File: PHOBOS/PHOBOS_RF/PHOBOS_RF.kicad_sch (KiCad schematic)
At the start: 0 parts

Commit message: RF Board schematic began
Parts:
- added AE1, AE2, AE3, AE4: Antenna, symbol Device:Antenna
- added J1: RF_IN, SMA_J_P_GF_RA_SM1:SAMTEC_SMA-J-P-GF-RA-SM1, symbol Connector:Conn_Coaxial
- added J7: Conn_01x05, Connector_JST:JST_PH_B5B-PH-K_1x05_P2.00mm_Vertical, symbol Connector_Generic:Conn_01x05
- added U1, U2, U3, U4: (no value), symbol JSPHS-2484+:JSPHS-2484+
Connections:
- new net: AE3.1 (A), U3.7 (RF_OUT)
- new net: AE1.1 (A), U1.7 (RF_OUT)
- new net: J1.1 (In), U1.1 (RF_IN), U2.1 (RF_IN), U3.1 (RF_IN), U4.1 (RF_IN)
- new net: AE2.1 (A), U2.7 (RF_OUT)
- new net: AE4.1 (A), U4.7 (RF_OUT)
- new net GND: J1.2 (Ext), J1.3, J1.4, J1.5, J7.5 (Pin_5), U1.10 (GND), U1.11 (GND), U1.12 (GND), U1.13 (GND), U1.14 (GND), U1.2 (GND), U1.3 (GND), U1.5 (GND), U1.8 (GND), U1.9 (GND), U2.10 (GND), U2.11 (GND), U2.12 (GND), U2.13 (GND), U2.14 (GND), U2.2 (GND), U2.3 (GND), U2.5 (GND), U2.8 (GND), U2.9 (GND), U3.10 (GND), U3.11 (GND), U3.12 (GND), U3.13 (GND), U3.14 (GND), U3.2 (GND), U3.3 (GND), U3.5 (GND), U3.8 (GND), U3.9 (GND), U4.10 (GND), U4.11 (GND), U4.12 (GND), U4.13 (GND), U4.14 (GND), U4.2 (GND), U4.3 (GND), U4.5 (GND), U4.8 (GND), U4.9 (GND)
- new net PS1: J7.1 (Pin_1), U1.4 (BIAS), U1.6 (BIAS)
- new net PS2: J7.2 (Pin_2), U2.4 (BIAS), U2.6 (BIAS)
- new net PS3: J7.3 (Pin_3), U3.4 (BIAS), U3.6 (BIAS)
- new net PS4: J7.4 (Pin_4), U4.4 (BIAS), U4.6 (BIAS)

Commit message: wilksinson schematic begun
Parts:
- added R1, R2, R3: 100, symbol Device:R
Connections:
- new net RF_IN: J1.1 (In), R1.1, R1.2, R2.1, R2.2, R3.1, R3.2
- now unconnected: U1.1 (RF_IN), U2.1 (RF_IN), U3.1 (RF_IN), U4.1 (RF_IN)
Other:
- moved on the sheet: J1, J7

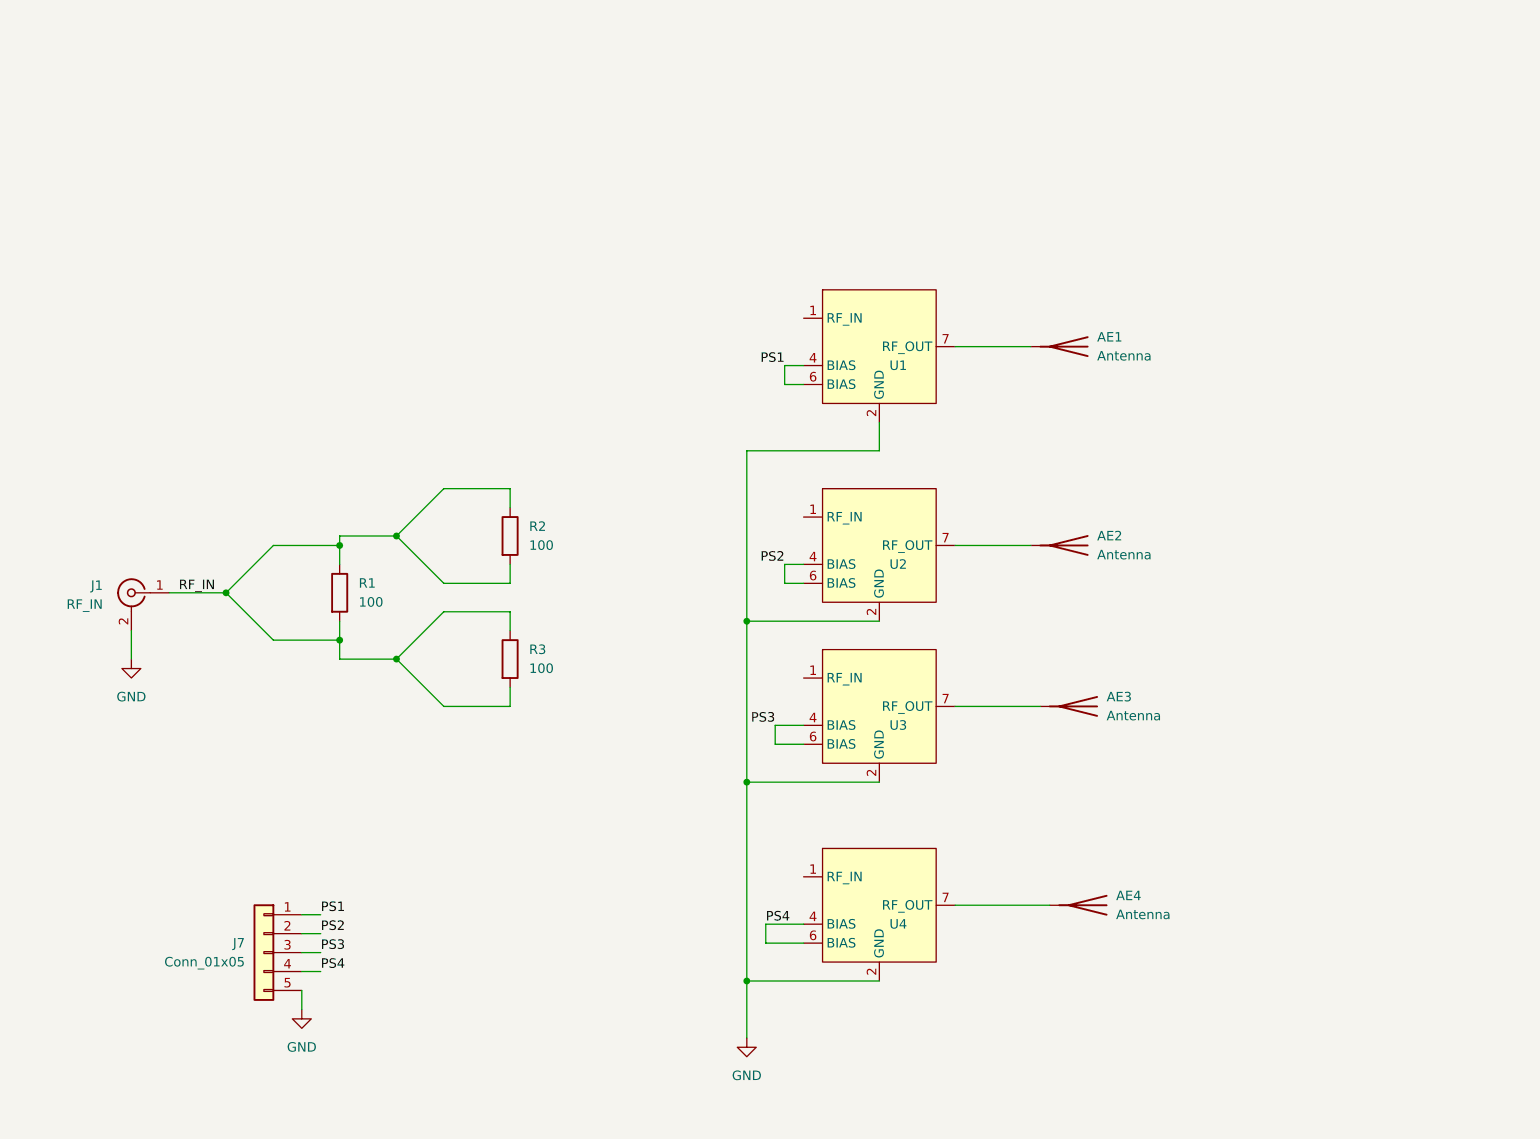
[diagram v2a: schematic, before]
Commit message: component wilkinson option added.
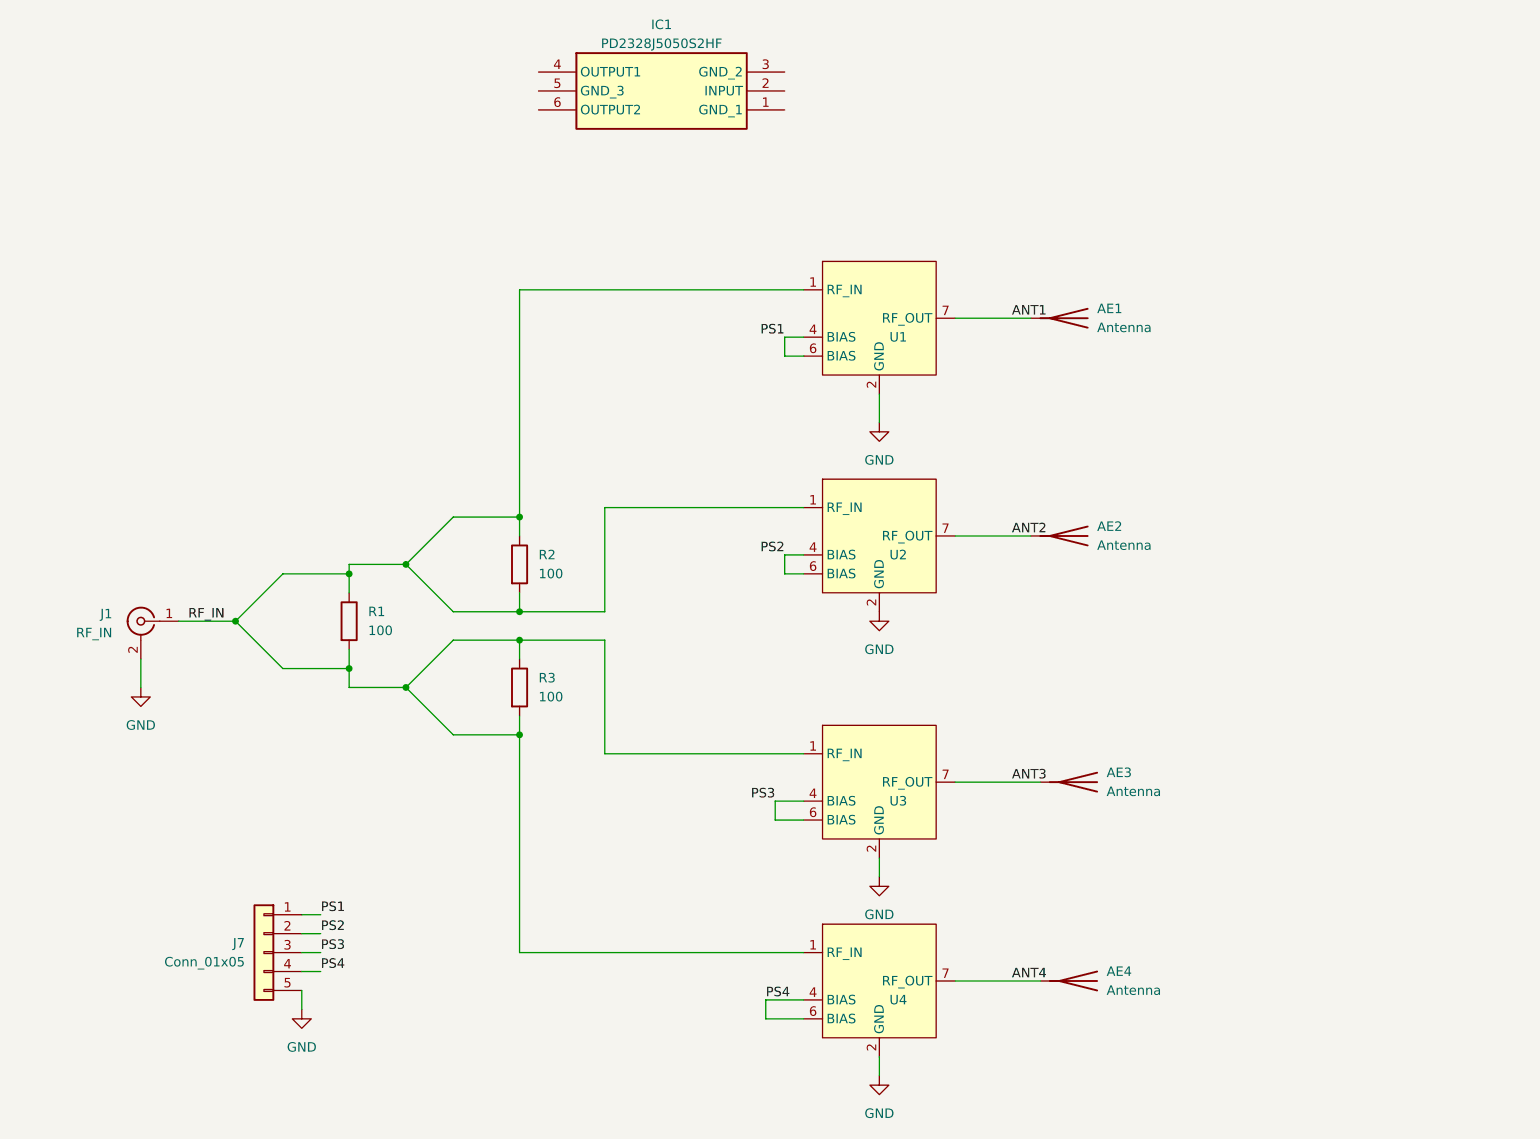
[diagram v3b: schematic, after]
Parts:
- added IC1: PD2328J5050S2HF, PD2328J5050S2HF, symbol PD2328J5050S2HF:PD2328J5050S2HF
- U1, U2, U3, U4: footprint (none) -> JSPHS-2484+:JSPHS2484
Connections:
- net RF_IN: now also U1.1 (RF_IN), U2.1 (RF_IN), U3.1 (RF_IN), U4.1 (RF_IN)
- net ANT3: now reaches AE3.1 (A), U3.7 (RF_OUT)
- net ANT1: now reaches AE1.1 (A), U1.7 (RF_OUT)
- net ANT2: now reaches AE2.1 (A), U2.7 (RF_OUT)
- net ANT4: now reaches AE4.1 (A), U4.7 (RF_OUT)
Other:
- moved on the sheet: AE1, AE2, AE3, AE4, J1, R1, R2, R3, U1, U2, U3, U4

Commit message: Divider Components added and wired
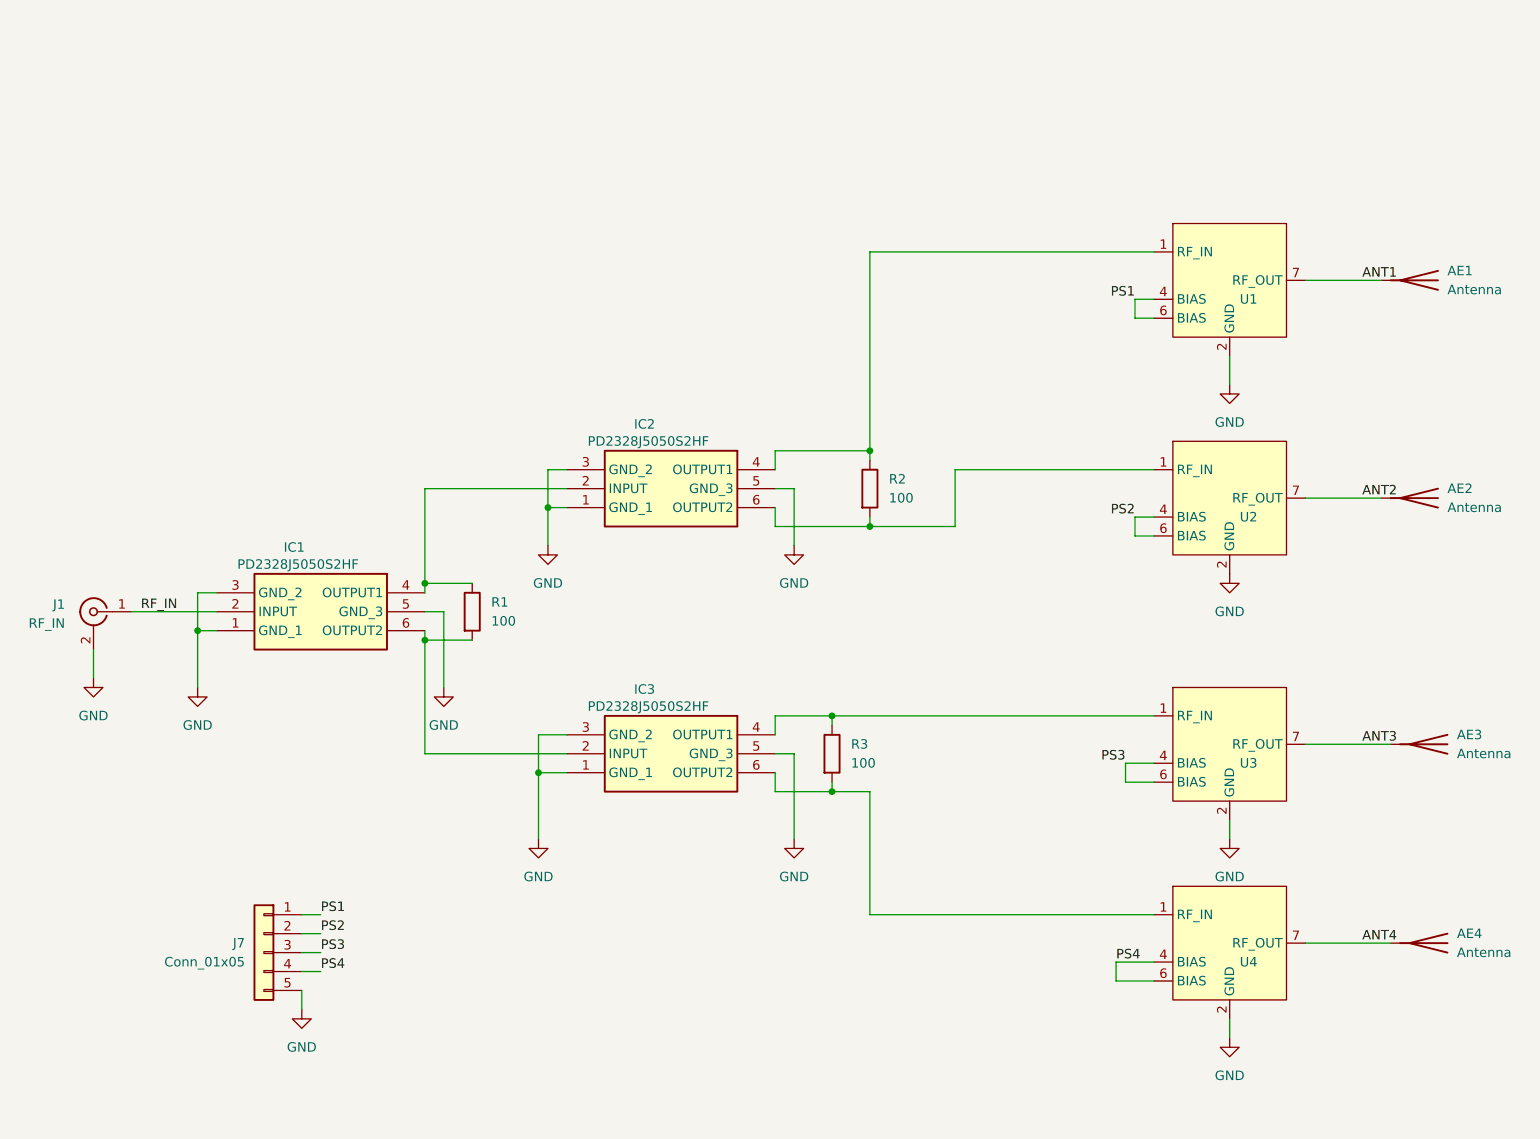
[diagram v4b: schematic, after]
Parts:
- added IC2, IC3: PD2328J5050S2HF, PD2328J5050S2HF:PD2328J5050S2HF, symbol PD2328J5050S2HF:PD2328J5050S2HF
- IC1: footprint PD2328J5050S2HF -> PD2328J5050S2HF:PD2328J5050S2HF
- R1, R2, R3: footprint (none) -> Resistor_SMD:R_0603_1608Metric
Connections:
- net GND: now also IC1.1 (GND_1), IC1.3 (GND_2), IC1.5 (GND_3), IC2.1 (GND_1), IC2.3 (GND_2), IC2.5 (GND_3), IC3.1 (GND_1), IC3.3 (GND_2), IC3.5 (GND_3)
- net RF_IN: now also IC1.2 (INPUT); no longer R1.1, R1.2, R2.1, R2.2, R3.1, R3.2, U1.1 (RF_IN), U2.1 (RF_IN), U3.1 (RF_IN), U4.1 (RF_IN)
- net at IC1.4 (OUTPUT1): now also R1.1, IC2.2 (INPUT)
- net at IC1.6 (OUTPUT2): now also R1.2, IC3.2 (INPUT)
- new net: IC2.4 (OUTPUT1), R2.1, U1.1 (RF_IN)
- new net: IC2.6 (OUTPUT2), R2.2, U2.1 (RF_IN)
- new net: IC3.4 (OUTPUT1), R3.1, U3.1 (RF_IN)
- new net: IC3.6 (OUTPUT2), R3.2, U4.1 (RF_IN)
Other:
- moved on the sheet: AE1, AE2, AE3, AE4, IC1, J1, U1, U2, U3, U4

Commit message: initial layout
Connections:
- net S1_OUT1: now reaches IC1.4 (OUTPUT1), IC2.2 (INPUT), R1.1
- net S1_OUT2: now reaches IC1.6 (OUTPUT2), IC3.2 (INPUT), R1.2
- net P1: now reaches IC2.4 (OUTPUT1), R2.1, U1.1 (RF_IN)
- net P2: now reaches IC2.6 (OUTPUT2), R2.2, U2.1 (RF_IN)
- net P3: now reaches IC3.4 (OUTPUT1), R3.1, U3.1 (RF_IN)
- net P4: now reaches IC3.6 (OUTPUT2), R3.2, U4.1 (RF_IN)
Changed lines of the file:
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@@
+		)
+	)
+	(label "P2"
+		(at 144.78 46.99 0)
+		(effects
+			(font
+				(size 1.27 1.27)
+			)
+			(justify left bottom)
 		)
 	)
@@
 	(label "ANT2"
 		(at 191.77 50.8 0)
+		(effects
+			(font
+				(size 1.27 1.27)
+			)
+			(justify left bottom)
+		)
+	)
+	(label "S1_OUT1"
+		(at 68.58 62.23 0)
 		(effects
 			(font
@@
 		)
 	)
+	(label "P3"
+		(at 144.78 80.01 0)
+		(effects
+			(font
+				(size 1.27 1.27)
+			)
+			(justify left bottom)
+		)
+	)
 	(label "PS4"
 		(at 158.75 113.03 0)
+		(effects
+			(font
+				(size 1.27 1.27)
+			)
+			(justify left bottom)
+		)
+	)
+	(label "P4"
+		(at 144.78 106.68 0)
 		(effects
 			(font
@@
 		)
 	)
+	(label "P1"
+		(at 144.78 17.78 0)
+		(effects
+			(font
+				(size 1.27 1.27)
+			)
+			(justify left bottom)
+		)
+	)
 	(label "ANT4"
 		(at 191.77 110.49 0)
 		(effects
 			(font
+				(size 1.27 1.27)
+			)
+			(justify left bottom)
+		)
+	)
+	(label "S1_OUT2"
+		(at 69.85 85.09 0)
+		(effects
+			(font
